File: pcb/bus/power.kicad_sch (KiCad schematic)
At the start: 15 parts, among them J401 Barrel_Jack_Switch, U401 TPS62933

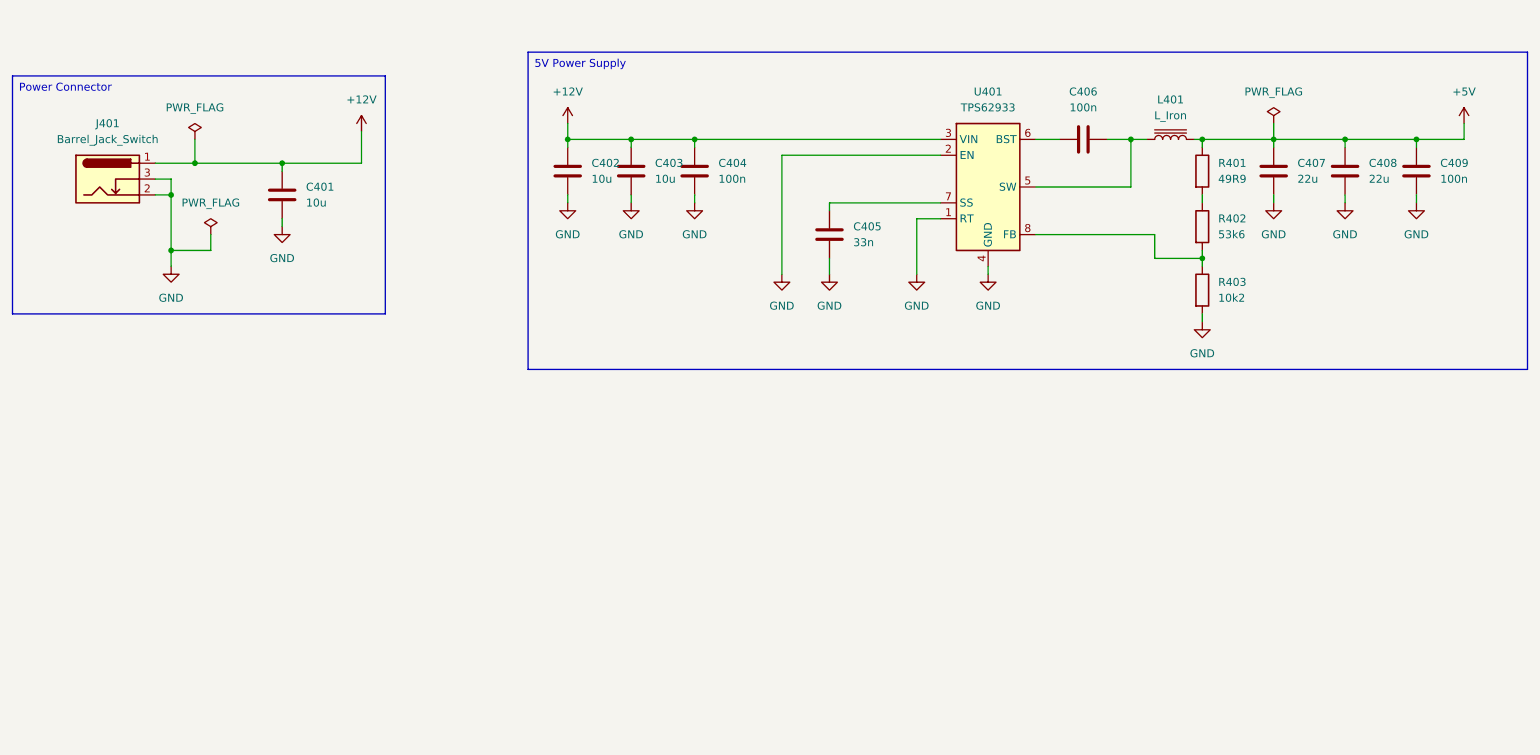
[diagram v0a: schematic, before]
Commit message: add leds
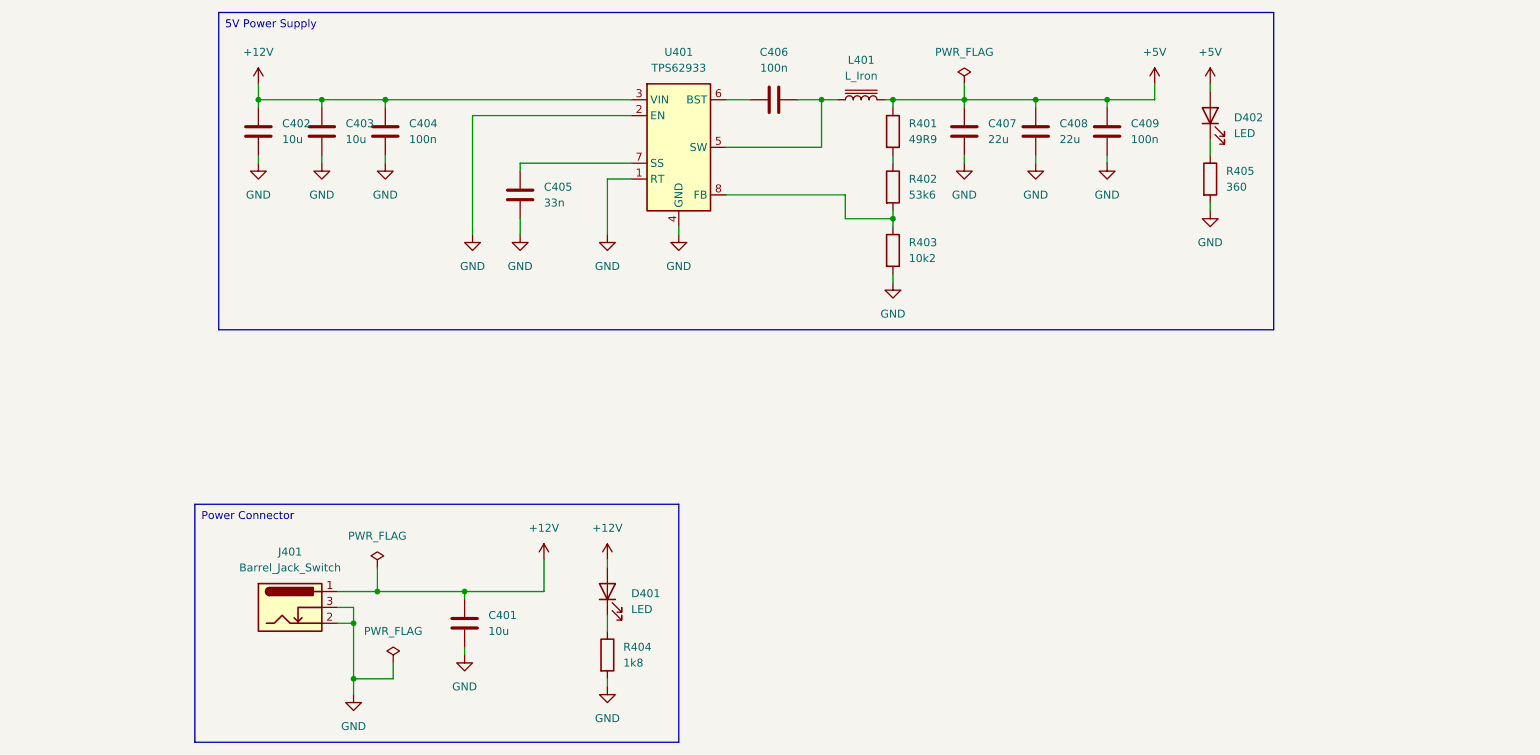
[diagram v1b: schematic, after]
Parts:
- added D401, D402: LED, symbol Device:LED
- added R404: 1k8, symbol Device:R
- added R405: 360, symbol Device:R
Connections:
- net +12V: now also D401.2 (A)
- net +5V: now also D402.2 (A)
- net GND: now also R404.2, R405.2
- new net: D402.1 (K), R405.1
- new net: D401.1 (K), R404.1
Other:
- moved on the sheet: C401, C402, C403, C404, C405, C406, C407, C408, C409, J401, L401, R401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
